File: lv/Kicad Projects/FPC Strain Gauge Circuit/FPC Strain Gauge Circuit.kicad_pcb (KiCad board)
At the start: 4 copper layers, 15 x 10 mm, 24 parts, among them U1 INA333xxDGK, U2 OPA333xxDBV, U3 ADS1220IRVAR

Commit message: Finish Circuit PCB
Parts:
- added ?: , , F.Cu at (122.4, 67.6)
- added ?: , , F.Cu at (124.0, 67.6)
- added ?: , , F.Cu at (125.5, 67.6)
- moved TP5 41.3 mm to (141.5, 67.8), turned to 90 degrees
- moved TP4 38.4 mm to (139.4, 67.8), turned to 90 degrees
- moved R5 36.5 mm to (123.4, 69.6), turned to -90 degrees
- moved TP3 35.6 mm to (137.4, 67.8), turned to 90 degrees
- moved R10 35.4 mm to (133.1, 71.6), turned to 90 degrees
- moved C8 34.9 mm to (141.2, 75.4), turned to 180 degrees
- moved C1 34.3 mm to (124.0, 71.1), turned to 180 degrees
- moved C7 34.1 mm to (141.2, 74.4), turned to 180 degrees
- moved C2 33.7 mm to (130.6, 68.6), turned to 90 degrees
- moved R6 33.5 mm to (124.5, 69.6), turned to -90 degrees
- moved TP2 33.0 mm to (135.4, 67.8), turned to 90 degrees
- moved C6 32.4 mm to (133.9, 69.8)
- moved TP1 30.5 mm to (133.3, 67.8), turned to 90 degrees
- moved R7 30.4 mm to (128.5, 69.1), turned to 180 degrees
- moved U3 30.2 mm to (139.2, 71.4)
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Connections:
- net /BRIDGE_N renamed R1
- net /BRIDGE_P renamed R2
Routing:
- net AGND: track 0.00 -> 31.9 mm, vias 0 -> 6
- net +3V3_A: track 0.00 -> 18.5 mm, vias 0 -> 4
- net /LOAD_SIGNAL: track 0.00 -> 14.1 mm, vias 0 -> 2
- net /VREF_1V65: track 0.00 -> 11.5 mm
- net /VREF_RAW: track 0.00 -> 7.08 mm
- net Net-(U1-+): track 0.00 -> 4.54 mm
- net Net-(U1--): track 0.00 -> 3.29 mm
- net R1: track 0.00 -> 3.25 mm
- net R2: track 0.00 -> 3.25 mm
- net Net-(R10-Pad1): track 0.00 -> 2.59 mm
- net /ADC_SCLK: track 0.00 -> 2.59 mm
- net /ADC_MISO: track 0.00 -> 2.51 mm
- net Net-(R7-Pad1): track 0.00 -> 2.27 mm
- net Net-(R7-Pad2): track 0.00 -> 2.27 mm
- net /ADC_MOSI: track 0.00 -> 1.87 mm
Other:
- board size 15 x 10 mm -> 22.6 x 10.5 mm

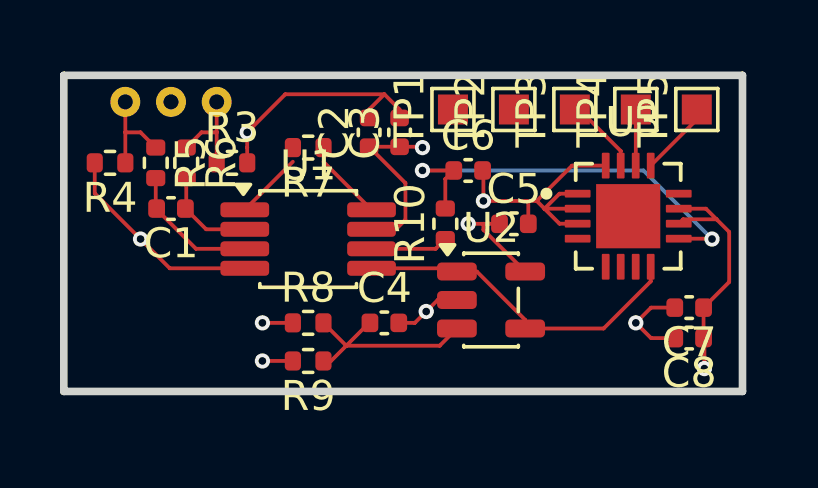
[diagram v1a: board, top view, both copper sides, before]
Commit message: Add old FPC files for reference and start work on new version
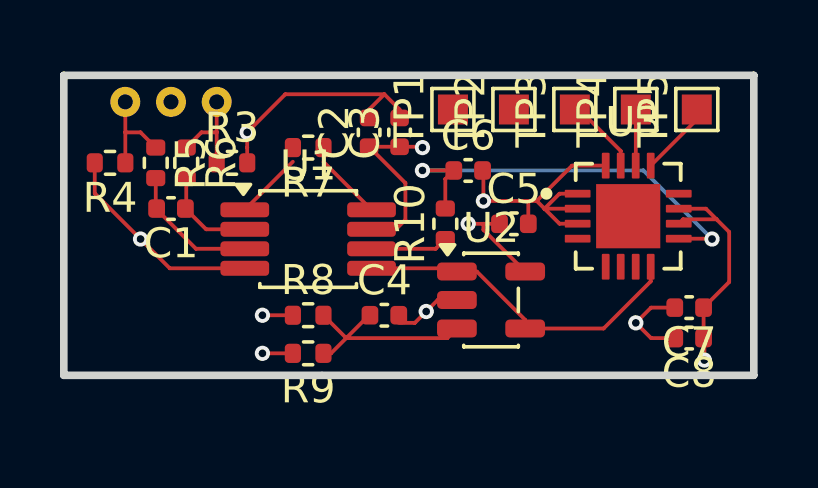
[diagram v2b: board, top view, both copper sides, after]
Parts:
- moved C4 0.25 mm to (131.1, 74.7)
- moved R8 0.25 mm to (128.5, 74.7)
- moved R9 0.25 mm to (128.5, 75.9)
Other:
- board size 22.6 x 10.5 mm -> 23 x 10 mm
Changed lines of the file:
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@@
 	(footprint "Capacitor_SMD:C_0402_1005Metric"
 		(layer "F.Cu")
-		(at 131.064 74.93)
+		(at 131.064 74.676)
 		(descr "Capacitor SMD 0402 (1005 Metric), square (rectangular) end terminal, IPC-7351 nominal, (Body size source: IPC-SM-782 page 76, https://www.pcb-3d.com/wordpress/wp-content/uploads/ipc-sm-782a_amendment_1_and_2.pdf)")
 		(tags "capacitor")
@@
 	(footprint "Resistor_SMD:R_0402_1005Metric"
 		(layer "F.Cu")
-		(at 128.524 74.93)
+		(at 128.524 74.676)
 		(descr "Resistor SMD 0402 (1005 Metric), square (rectangular) end terminal, IPC-7351 nominal, (Body size source: IPC-SM-782 page 72, https://www.pcb-3d.com/wordpress/wp-content/uploads/ipc-sm-782a_amendment_1_and_2.pdf)")
 		(tags "resistor")
@@
 	(footprint "Resistor_SMD:R_0402_1005Metric"
 		(layer "F.Cu")
-		(at 128.524 76.2 180)
+		(at 128.524 75.946 180)
 		(descr "Resistor SMD 0402 (1005 Metric), square (rectangular) end terminal, IPC-7351 nominal, (Body size source: IPC-SM-782 page 72, https://www.pcb-3d.com/wordpress/wp-content/uploads/ipc-sm-782a_amendment_1_and_2.pdf)")
 		(tags "resistor")
@@
 	(gr_rect
 		(start 120.379 66.679)
-		(end 143.002 77.216)
+		(end 143.379 76.679)
 		(stroke
 			(width 0.254)
@@
 	)
 	(segment
-		(start 127 76.2)
-		(end 128.014 76.2)
+		(start 127 75.946)
+		(end 128.014 75.946)
 		(width 0.127)
 		(layer "F.Cu")
@@
 	)
 	(via
-		(at 127 76.2)
+		(at 127 75.946)
 		(size 0.508)
 		(drill 0.254)
@@
 	)
 	(segment
-		(start 129.034 74.93)
-		(end 129.034 74.932)
+		(start 133.1625 75.438)
+		(end 133.4825 75.118)
 		(width 0.127)
 		(layer "F.Cu")
@@
 	)
 	(segment
-		(start 129.286 76.2)
-		(end 129.794 75.692)
+		(start 129.034 74.676)
+		(end 129.034 74.678)
 		(width 0.127)
 		(layer "F.Cu")
@@
 	)
 	(segment
-		(start 129.034 74.932)
-		(end 129.794 75.692)
+		(start 129.794 75.438)
+		(end 133.1625 75.438)
 		(width 0.127)
 		(layer "F.Cu")
@@
 	)
 	(segment
-		(start 132.9085 75.692)
-		(end 129.794 75.692)
+		(start 129.286 75.946)
+		(end 129.794 75.438)
 		(width 0.127)
 		(layer "F.Cu")
@@
 	)
 	(segment
-		(start 130.584 74.93)
-		(end 130.556 74.93)
+		(start 129.034 74.678)
+		(end 129.794 75.438)
 		(width 0.127)
 		(layer "F.Cu")
@@
 	)
 	(segment
-		(start 133.4825 75.118)
-		(end 132.9085 75.692)
+		(start 130.584 74.676)
+		(end 130.556 74.676)
 		(width 0.127)
 		(layer "F.Cu")
@@
 	)
 	(segment
-		(start 129.034 76.2)
-		(end 129.286 76.2)
+		(start 129.034 75.946)
+		(end 129.286 75.946)
 		(width 0.127)
 		(layer "F.Cu")
@@
 	)
 	(segment
-		(start 130.556 74.93)
-		(end 129.794 75.692)
+		(start 130.556 74.676)
+		(end 129.794 75.438)
 		(width 0.127)
 		(layer "F.Cu")
@@
 	)
 	(segment
-		(start 134.366 71.628)
-		(end 133.858 71.628)
+		(start 141.732 75.466)
+		(end 141.704 75.438)
 		(width 0.127)
 		(layer "F.Cu")
@@
 	)
 	(segment
-		(start 142.5575 71.899276)
-		(end 142.136112 71.477888)
+		(start 134.366 71.628)
+		(end 133.858 71.628)
 		(width 0.127)
 		(layer "F.Cu")
@@
 	)
 	(segment
-		(start 141.732 76.454)
-		(end 141.732 75.466)
+		(start 142.5575 71.899276)
+		(end 142.136112 71.477888)
 		(width 0.127)
 		(layer "F.Cu")
@@
 	)
 	(segment
-		(start 127 74.93)
-		(end 128.014 74.93)
+		(start 127 74.676)
+		(end 128.014 74.676)
 		(width 0.127)
 		(layer "F.Cu")
@@
 	)
 	(segment
-		(start 141.732 75.466)
-		(end 141.704 75.438)
+		(start 134.902 71.628)
+		(end 134.366 71.628)
 		(width 0.127)
 		(layer "F.Cu")
@@
 	)
 	(segment
-		(start 134.902 71.628)
-		(end 134.366 71.628)
+		(start 131.7665 71.493499)
+		(end 131.448999 71.811)
 		(width 0.127)
 		(layer "F.Cu")
@@
 	)
 	(segment
-		(start 131.7665 71.493499)
-		(end 131.448999 71.811)
+		(start 141.732 76.171)
+		(end 141.732 75.466)
 		(width 0.127)
 		(layer "F.Cu")
@@
 	)
 	(via
-		(at 127 74.93)
+		(at 127 74.676)
 		(size 0.508)
 		(drill 0.254)
@@
 	)
 	(via
-		(at 141.732 76.454)
+		(at 141.732 76.171)
 		(size 0.508)
 		(drill 0.254)
